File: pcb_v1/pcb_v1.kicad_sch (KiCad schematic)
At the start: 15 parts, among them J1 Conn_01x04, SW1 RotaryEncoder, SW2 SW_Push, U1 STM32WB5MMG, U2 SRV05-4

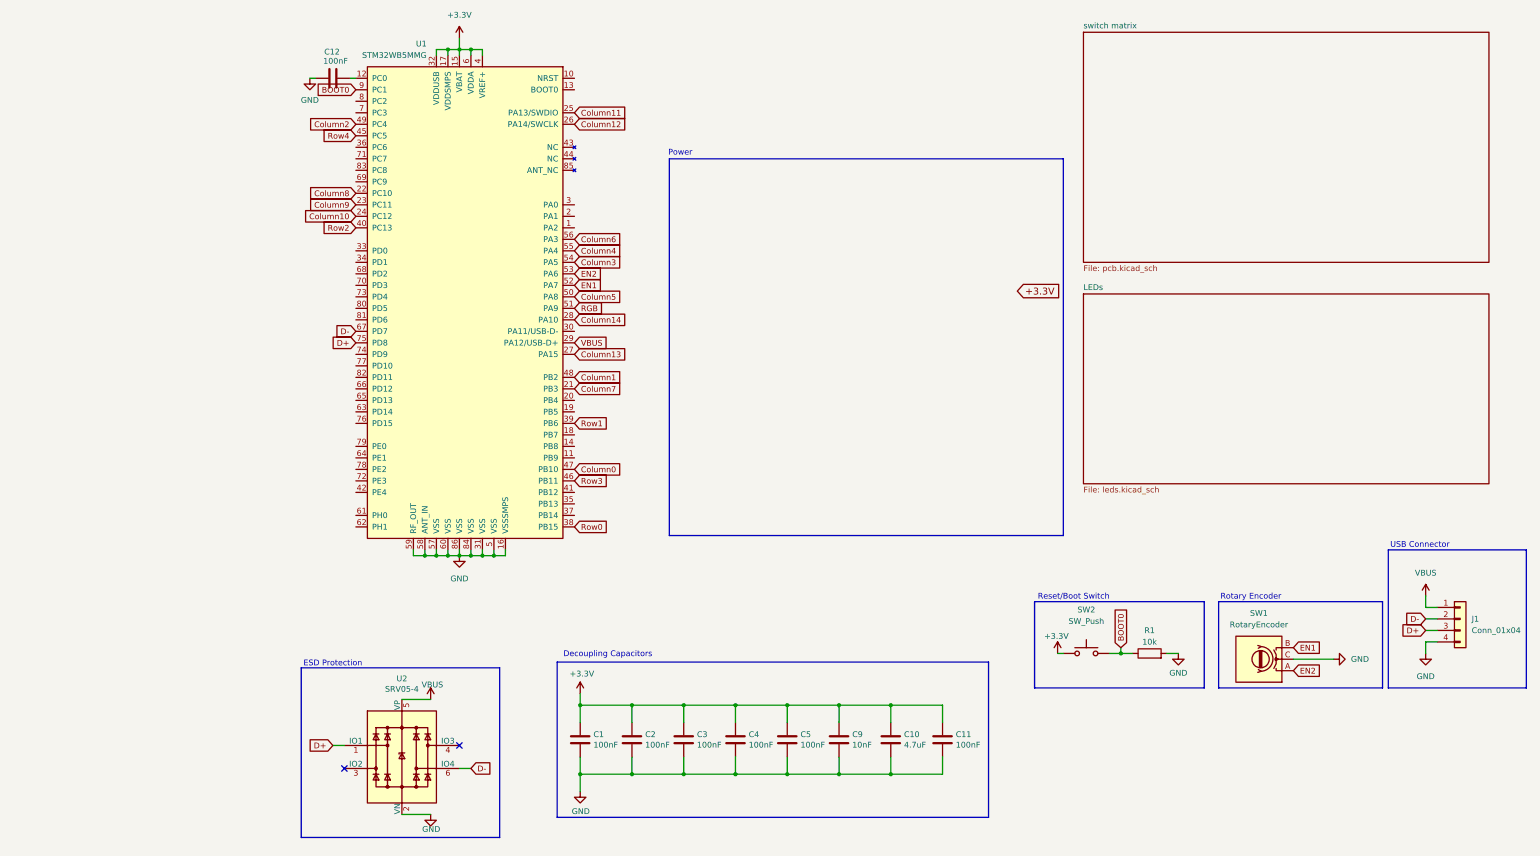
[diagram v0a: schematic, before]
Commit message: Wiring Update
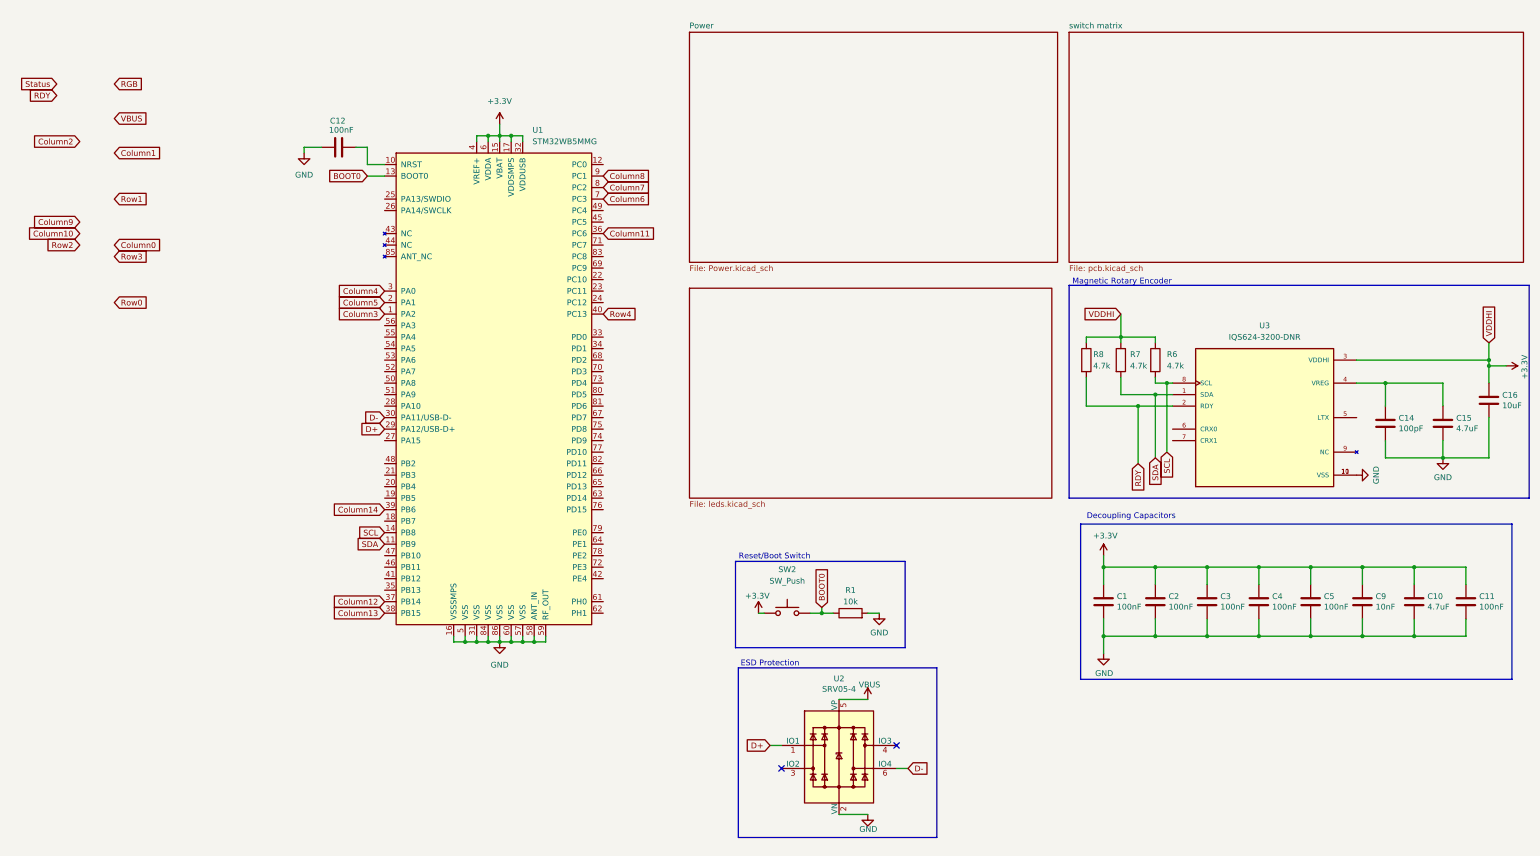
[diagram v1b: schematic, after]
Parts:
- removed J1: Conn_01x04, Connector_JST:JST_SH_SM04B-SRSS-TB_1x04-1MP_P1.00mm_Horizontal, symbol Connector_Generic:Conn_01x04
- removed SW1: RotaryEncoder, My_Footprints:EN05VS1212NHH, symbol Device:RotaryEncoder
- added C14: 100pF, Capacitor_SMD:C_0805_2012Metric, symbol Device:C
- added C15: 4.7uF, Capacitor_SMD:C_0805_2012Metric, symbol Device:C
- added C16: 10uF, Capacitor_SMD:C_0805_2012Metric, symbol Device:C
- added R6, R7, R8: 4.7k, symbol Device:R
- added U3: IQS624-3200-DNR, IQS624-3200-DNR:SON50P300X300X80-11N, symbol IQS624-3200-DNR:IQS624-3200-DNR
- SW2: footprint (none) -> ScottoKeebs_Components:Button_TL3342
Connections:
- net +3.3V: now also C16.1, R6.1, R7.1, R8.1, U3.3 (VDDHI)
- net BOOT0: now also U1.13 (BOOT0); no longer U1.9 (PC1)
- net Column0: no longer U1.47 (PB10)
- net Column1: no longer U1.48 (PB2)
- net Column10: no longer U1.24 (PC12)
- net Column11: now also U1.36 (PC6); no longer U1.25 (PA13/SWDIO)
- net Column12: now also U1.37 (PB14); no longer U1.26 (PA14/SWCLK)
- net Column13: now also U1.38 (PB15); no longer U1.27 (PA15)
- net Column14: now also U1.39 (PB6); no longer U1.28 (PA10)
- net Column2: no longer U1.49 (PC4)
- net Column3: now also U1.1 (PA2); no longer U1.54 (PA5)
- net Column4: now also U1.3 (PA0); no longer U1.55 (PA4)
- net Column5: now also U1.2 (PA1); no longer U1.50 (PA8)
- net Column6: now also U1.7 (PC3); no longer U1.56 (PA3)
- net Column7: now also U1.8 (PC2); no longer U1.21 (PB3)
- net Column8: now also U1.9 (PC1); no longer U1.22 (PC10)
- net Column9: no longer U1.23 (PC11)
- net D+: now also U1.29 (PA12/USB-D+); no longer U1.75 (PD8)
- net D-: now also U1.30 (PA11/USB-D-); no longer U1.67 (PD7)
- net GND: now also C14.2, C15.2, C16.2, U3.10 (VSS), U3.11 (VSS)
- net RGB: no longer U1.51 (PA9)
- net Row0: no longer U1.38 (PB15)
- net Row1: no longer U1.39 (PB6)
- net Row2: no longer U1.40 (PC13)
- net Row3: no longer U1.46 (PB11)
- net Row4: now also U1.40 (PC13); no longer U1.45 (PC5)
- net VBUS: no longer U1.29 (PA12/USB-D+)
- net at C12.2: now also U1.10 (NRST); no longer U1.12 (PC0)
- net SDA: now reaches U1.11 (PB9)
- net SDA: now also R7.2, U3.1 (SDA)
- net SCL: now reaches U1.14 (PB8)
- net SCL: now also R6.2, U3.8 (SCL)
- net EN1: no longer names the net of U1.52 (PA7)
- net EN2: no longer names the net of U1.53 (PA6)
- new net: C14.1, C15.1, U3.4 (VREG)
- new net RDY: R8.2, U3.2 (RDY)
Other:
- added sheet Power (Power.kicad_sch)
- note added: "Magnetic Rotary Encoder"
- note removed: "Power"
- note removed: "Rotary Encoder"
- note removed: "USB Connector"
- moved on the sheet: C1, C10, C11, C12, C2, C3, C4, C5, C9, R1, SW2, U1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

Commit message: New MCU. Added ESP32 S3 Mini1 to act as Bluetooth module
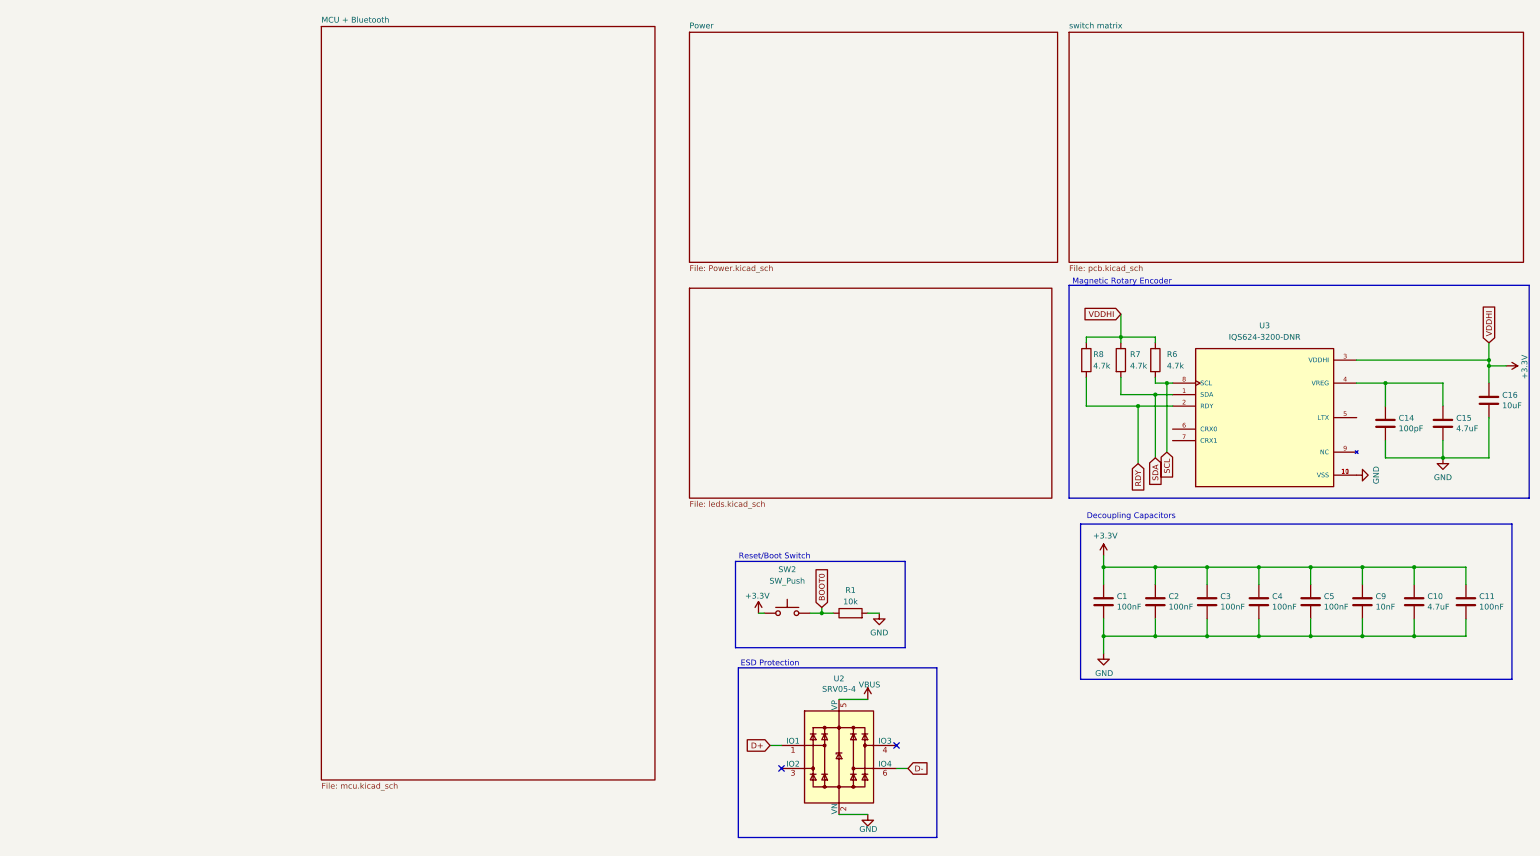
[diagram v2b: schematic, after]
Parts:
- removed C12: 100nF, Capacitor_SMD:C_0805_2012Metric, symbol Device:C
- removed U1: STM32WB5MMG, PCM_marbastlib-xp-various:STM32WB5MMG, symbol PCM_marbastlib-various:STM32WB5MMG
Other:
- added sheet MCU + Bluetooth (mcu.kicad_sch)

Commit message: Updated wiring
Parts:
- C1, C10, C11, C14, C15, C16, C2, C3, C4, C5, C9: footprint Capacitor_SMD:C_0805_2012Metric -> Murata Capacitor:CAPC1608X90N
- R1, R6, R7, R8: footprint (none) -> Yageo Resistor:RESC1607X60N
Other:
- moved on the sheet: R1, SW2
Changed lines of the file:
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@@
 	)
 	(rectangle
-		(start 109.22 135.89)
-		(end 146.685 154.94)
+		(start 93.98 134.62)
+		(end 131.445 153.67)
 		(stroke
 			(width 0)
@@
 	(text "Reset/Boot Switch"
 		(exclude_from_sim no)
-		(at 117.856 134.874 0)
+		(at 102.616 133.604 0)
 		(effects
 			(font
@@
 	)
 	(junction
+		(at 199.39 101.6)
+		(diameter 0)
+		(color 0 0 0 0)
+	)
+	(junction
 		(at 259.08 137.16)
 		(diameter 0)
@@
 	)
 	(junction
-		(at 128.27 147.32)
+		(at 113.03 146.05)
 		(diameter 0)
 		(color 0 0 0 0)
@@
 	)
 	(junction
-		(at 198.12 101.6)
-		(diameter 0)
-		(color 0 0 0 0)
-	)
-	(junction
 		(at 265.43 113.03)
 		(diameter 0)
@@
 	(wire
 		(pts
-			(xy 205.74 101.6) (xy 198.12 101.6)
+			(xy 205.74 101.6) (xy 199.39 101.6)
 		)
 		(stroke
@@
 	(wire
 		(pts
+			(xy 265.43 114.3) (xy 265.43 113.03)
+		)
+		(stroke
+			(width 0)
+			(type default)
+		)
+	)
+	(wire
+		(pts
 			(xy 190.5 152.4) (xy 190.5 156.21)
 		)
@@
 	(wire
 		(pts
-			(xy 198.12 101.6) (xy 186.69 101.6)
+			(xy 186.69 101.6) (xy 199.39 101.6)
 		)
 		(stroke
@@
 	(wire
 		(pts
-			(xy 128.27 147.32) (xy 130.81 147.32)
+			(xy 113.03 146.05) (xy 115.57 146.05)
 		)
 		(stroke
@@
 	(wire
 		(pts
-			(xy 128.27 146.05) (xy 128.27 147.32)
+			(xy 113.03 144.78) (xy 113.03 146.05)
 		)
 		(stroke
@@
 	(wire
 		(pts
-			(xy 138.43 147.32) (xy 140.97 147.32)
+			(xy 123.19 146.05) (xy 125.73 146.05)
 		)
 		(stroke
@@
 	(wire
 		(pts
-			(xy 198.12 101.6) (xy 198.12 114.3)
+			(xy 199.39 101.6) (xy 199.39 114.3)
 		)
 		(stroke
@@
 	(wire
 		(pts
-			(xy 125.73 147.32) (xy 128.27 147.32)
+			(xy 110.49 146.05) (xy 113.03 146.05)
 		)
 		(stroke
@@
 	(wire
 		(pts
-			(xy 114.3 147.32) (xy 115.57 147.32)
+			(xy 99.06 146.05) (xy 100.33 146.05)
 		)
 		(stroke
@@
 	(global_label "RDY"
 		(shape input)
-		(at 198.12 114.3 270)
+		(at 199.39 114.3 270)
 		(fields_autoplaced yes)
 		(effects
@@
 		)
 		(property "Intersheetrefs" "${INTERSHEET_REFS}"
-			(at 198.12 120.9138 90)
+			(at 199.39 120.9138 90)
 			(effects
 				(font
@@
 	(global_label "BOOT0"
 		(shape input)
-		(at 128.27 146.05 90)
+		(at 113.03 144.78 90)
 		(fields_autoplaced yes)
 		(effects
@@
 		)
 		(property "Intersheetrefs" "${INTERSHEET_REFS}"
-			(at 128.27 136.9567 90)
+			(at 113.03 135.6867 90)
 			(effects
 				(font
@@
 			)
 		)
-		(property "Footprint" "Capacitor_SMD:C_0805_2012Metric"
+		(property "Footprint" "Murata Capacitor:CAPC1608X90N"
 			(at 191.4652 148.59 0)
 			(effects
@@
 			)
 		)
-		(property "Footprint" "Capacitor_SMD:C_0805_2012Metric"
+		(property "Footprint" "Murata Capacitor:CAPC1608X90N"
 			(at 214.3252 148.59 0)
 			(effects
@@
 			)
 		)
-		(property "Footprint" "Capacitor_SMD:C_0805_2012Metric"
+		(property "Footprint" "Murata Capacitor:CAPC1608X90N"
 			(at 237.1852 148.59 0)
 			(effects
@@
 	(symbol
 		(lib_id "power:GND")
-		(at 140.97 147.32 0)
+		(at 125.73 146.05 0)
 		(unit 1)
 		(exclude_from_sim no)
@@
 		(dnp no)
 		(property "Reference" "#PWR015"
-			(at 140.97 153.67 0)
+			(at 125.73 152.4 0)
 			(effects
 				(font
@@
 		)
 		(property "Value" "GND"
-			(at 140.97 151.638 0)
+			(at 125.73 150.368 0)
 			(effects
 				(font
@@
 		)
 		(property "Footprint" ""
-			(at 140.97 147.32 0)
+			(at 125.73 146.05 0)
 			(effects
 				(font
@@
 		)
 		(property "Datasheet" ""
-			(at 140.97 147.32 0)
+			(at 125.73 146.05 0)
 			(effects
 				(font
@@
 		)
 		(property "Description" ""
-			(at 140.97 147.32 0)
+			(at 125.73 146.05 0)
 			(effects
 				(font
@@
 	(symbol
 		(lib_id "power:GND")
-		(at 265.43 113.03 0)
+		(at 265.43 114.3 0)
 		(unit 1)
 		(exclude_from_sim no)
@@
 		(dnp no)
 		(property "Reference" "#PWR020"
-			(at 265.43 119.38 0)
+			(at 265.43 120.65 0)
 			(effects
 				(font
@@
 		)
 		(property "Value" "GND"
-			(at 265.43 117.348 0)
+			(at 265.43 118.618 0)
 			(effects
 				(font
@@
 		)
 		(property "Footprint" ""
-			(at 265.43 113.03 0)
+			(at 265.43 114.3 0)
 			(effects
 				(font
@@
 		)
 		(property "Datasheet" ""
-			(at 265.43 113.03 0)
+			(at 265.43 114.3 0)
 			(effects
 				(font
@@
 		)
 		(property "Description" ""
-			(at 265.43 113.03 0)
+			(at 265.43 114.3 0)
 			(effects
 				(font
@@
 	(symbol
 		(lib_id "Switch:SW_Push")
-		(at 120.65 147.32 0)
+		(at 105.41 146.05 0)
 		(unit 1)
 		(exclude_from_sim no)
@@
 		(dnp no)
 		(property "Reference" "SW2"
-			(at 120.65 137.668 0)
+			(at 105.41 136.398 0)
 			(effects
 				(font
@@
 		)
 		(property "Value" "SW_Push"
-			(at 120.65 140.208 0)
+			(at 105.41 138.938 0)
 			(effects
 				(font
@@
 		)
 		(property "Footprint" "ScottoKeebs_Components:Button_TL3342"
-			(at 120.65 142.24 0)
+			(at 105.41 140.97 0)
 			(effects
 				(font
@@
 		)
 		(property "Datasheet" "~"
-			(at 120.65 142.24 0)
+			(at 105.41 140.97 0)
 			(effects
 				(font
@@
 		)
 		(property "Description" "Push button switch, generic, two pins"
-			(at 120.65 147.32 0)
+			(at 105.41 146.05 0)
 			(effects
 				(font
@@
 	(symbol
 		(lib_id "ScottoKeebs:Placeholder_Resistor")
-		(at 134.62 147.32 0)
+		(at 119.38 146.05 0)
 		(unit 1)
 		(exclude_from_sim no)
@@
 		(dnp no)
 		(property "Reference" "R1"
-			(at 134.62 142.24 0)
+			(at 119.38 140.97 0)
 			(effects
 				(font
@@
 		)
 		(property "Value" "10k"
-			(at 134.62 144.78 0)
+			(at 119.38 143.51 0)
 			(effects
 				(font
@@
 			)
 		)
-		(property "Footprint" ""
-			(at 134.62 149.098 0)
+		(property "Footprint" "Yageo Resistor:RESC1607X60N"
+			(at 119.38 147.828 0)
 			(effects
 				(font
@@
 		)
 		(property "Datasheet" "~"
-			(at 134.62 147.32 90)
+			(at 119.38 146.05 90)
 			(effects
 				(font
@@
 		)
 		(property "Description" "Resistor"
-			(at 134.62 147.32 0)
+			(at 119.38 146.05 0)
 			(effects
 				(font
@@
 			)
 		)
-		(property "Footprint" "Capacitor_SMD:C_0805_2012Metric"
+		(property "Footprint" "Murata Capacitor:CAPC1608X90N"
 			(at 271.4752 148.59 0)
 			(effects
@@
 			)
 		)
-		(property "Footprint" "Capacitor_SMD:C_0805_2012Metric"
+		(property "Footprint" "Murata Capacitor:CAPC1608X90N"
 			(at 248.6152 148.59 0)
 			(effects
@@
 			)
 		)
-		(property "Footprint" "Capacitor_SMD:C_0805_2012Metric"
+		(property "Footprint" "Murata Capacitor:CAPC1608X90N"
 			(at 266.3952 109.22 0)
 			(effects
@@
 	(symbol
 		(lib_id "power:+3.3V")
-		(at 114.3 147.32 0)
+		(at 99.06 146.05 0)
 		(unit 1)
 		(exclude_from_sim no)
@@
 		(dnp no)
 		(property "Reference" "#PWR014"
-			(at 114.3 151.13 0)
+			(at 99.06 149.86 0)
 			(effects
 				(font
@@
 		)
 		(property "Value" "+3.3V"
-			(at 114.046 143.51 0)
+			(at 98.806 142.24 0)
 			(effects
 				(font
@@
 		)
 		(property "Footprint" ""
-			(at 114.3 147.32 0)
+			(at 99.06 146.05 0)
 			(effects
 				(font
@@
 		)
 		(property "Datasheet" ""
-			(at 114.3 147.32 0)
+			(at 99.06 146.05 0)
 			(effects
 				(font
@@
 		)
 		(property "Description" "Power symbol creates a global label with name \"+3.3V\""
-			(at 114.3 147.32 0)
+			(at 99.06 146.05 0)
 			(effects
 				(font
@@
 			)
 		)
-		(property "Footprint" ""
+		(property "Footprint" "Yageo Resistor:RESC1607X60N"
 			(at 200.152 91.44 90)
 			(effects
@@
 			)
 		)
-		(property "Footprint" "Capacitor_SMD:C_0805_2012Metric"
+		(property "Footprint" "Murata Capacitor:CAPC1608X90N"
 			(at 276.5552 104.14 0)
 			(effects
@@
 			)
 		)
-		(property "Footprint" "Capacitor_SMD:C_0805_2012Metric"
+		(property "Footprint" "Murata Capacitor:CAPC1608X90N"
 			(at 253.6952 109.22 0)
 			(effects
@@
 			)
 		)
-		(property "Footprint" "Capacitor_SMD:C_0805_2012Metric"
+		(property "Footprint" "Murata Capacitor:CAPC1608X90N"
 			(at 225.7552 148.59 0)
 			(effects
@@
 			)
 		)
-		(property "Footprint" "Capacitor_SMD:C_0805_2012Metric"
+		(property "Footprint" "Murata Capacitor:CAPC1608X90N"
 			(at 260.0452 148.59 0)
 			(effects
@@
 			)
 		)
-		(property "Footprint" ""
+		(property "Footprint" "Yageo Resistor:RESC1607X60N"
 			(at 184.912 91.44 90)
 			(effects
@@
 			)
 		)
-		(property "Footprint" "Capacitor_SMD:C_0805_2012Metric"
+		(property "Footprint" "Murata Capacitor:CAPC1608X90N"
 			(at 202.8952 148.59 0)
 			(effects
@@
 			)
 		)
-		(property "Footprint" ""
+		(property "Footprint" "Yageo Resistor:RESC1607X60N"
 			(at 192.532 91.44 90)
 			(effects
@@
 	)
 	(sheet
-		(at 17.78 17.78)
-		(size 73.66 166.37)
+		(at 17.78 19.05)
+		(size 73.66 176.53)
 		(exclude_from_sim no)
 		(in_bom yes)
@@
 		)
 		(property "Sheetname" "MCU + Bluetooth"
-			(at 17.78 17.0684 0)
+			(at 17.78 18.3384 0)
 			(effects
 				(font
@@
 		)
 		(property "Sheetfile" "mcu.kicad_sch"
-			(at 17.78 184.7346 0)
+			(at 17.78 196.1646 0)
 			(effects
 				(font

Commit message: Update Wiring
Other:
- note added: "Boot Switch"
- note removed: "Reset/Boot Switch"
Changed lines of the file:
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@@
 		)
 	)
-	(text "Reset/Boot Switch"
+	(text "Boot Switch"
 		(exclude_from_sim no)
-		(at 102.616 133.604 0)
+		(at 99.568 133.604 0)
 		(effects
 			(font
